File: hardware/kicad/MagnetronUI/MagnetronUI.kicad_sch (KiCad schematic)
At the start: 10 parts, among them J1 Conn_01x04, J2 Conn_02x13_Counter_Clockwise, SW1 SW_Push, SW2 SW_Push

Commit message: feat: cleanup
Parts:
- removed C1, C2: C, Capacitor_SMD:C_0805_2012Metric_Pad1.18x1.45mm_HandSolder, symbol Device:C
- removed R1, R2, R3, R4: R, Resistor_SMD:R_0805_2012Metric_Pad1.20x1.40mm_HandSolder, symbol Device:R
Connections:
- net aux1_btn: now also SW2.1
- net aux2_btn: now also SW1.1

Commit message: feat: updates
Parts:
- removed SW2: SW_Push, TerminalBlock_Phoenix:TerminalBlock_Phoenix_MKDS-1,5-2_1x02_P5.00mm_Horizontal, symbol Switch:SW_Push
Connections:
- net aux2_btn is gone; now on net aux1_btn: J2.18 (Pin_18), SW1.1
- net +3.3V: no longer J1.2 (Pin_2)
- net aux1_btn: no longer J2.17 (Pin_17)
- net +5V: now reaches J2.22 (Pin_22)
- net +5V: now also J1.2 (Pin_2)

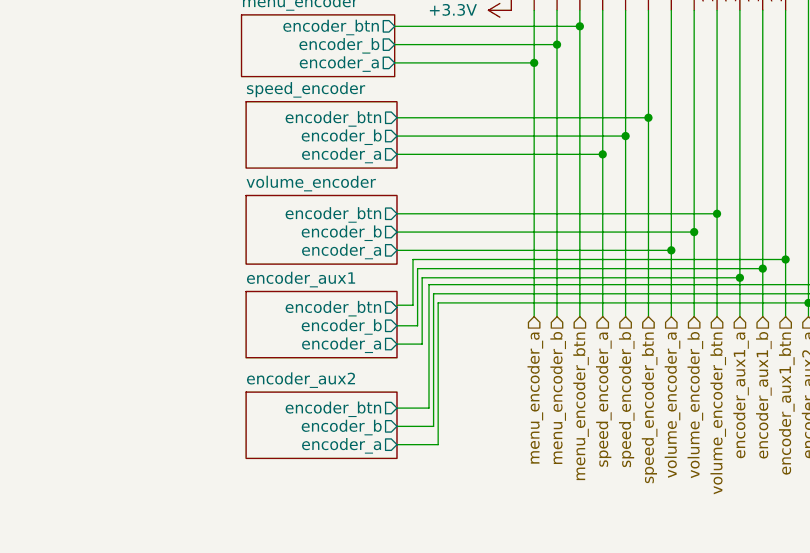
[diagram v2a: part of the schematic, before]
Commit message: feat: update to 2 layer board
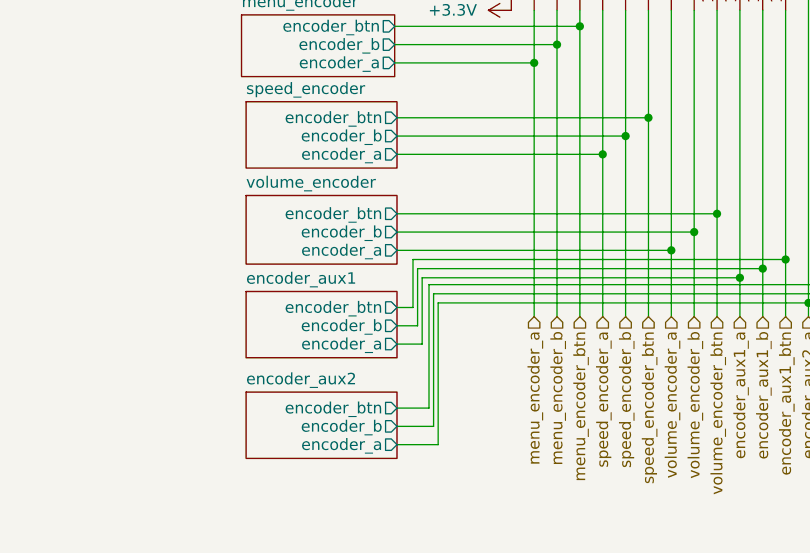
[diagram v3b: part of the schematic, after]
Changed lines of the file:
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@@
+	(wire
+		(pts
+			(xy 84.836 116.586) (xy 84.836 121.92)
+		)
+		(stroke
+			(width 0)
+			(type default)
+		)
+	)
 	(wire
 		(pts
@@
 	(wire
 		(pts
-			(xy 83.058 121.666) (xy 84.836 121.666)
-		)
-		(stroke
-			(width 0)
-			(type default)
-		)
-	)
-	(wire
-		(pts
 			(xy 144.018 122.936) (xy 144.018 60.96)
 		)
@@
 	(wire
 		(pts
+			(xy 83.058 121.92) (xy 84.836 121.92)
+		)
+		(stroke
+			(width 0)
+			(type default)
+		)
+	)
+	(wire
+		(pts
 			(xy 118.618 111.506) (xy 118.618 122.936)
 		)
@@
 		)
 		(stroke
-			(width 0)
-			(type default)
-		)
-	)
-	(wire
-		(pts
-			(xy 84.836 121.666) (xy 84.836 116.586)
-		)
-		(stroke

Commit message: chore: cleanup/mounting holes
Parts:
- added H1, H2, H3, H4: MountingHole_Pad, MountingHole:MountingHole_3.2mm_M3_ISO7380_Pad_TopBottom, symbol Mechanical:MountingHole_Pad
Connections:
- net GND: now also H1.1, H2.1, H3.1, H4.1

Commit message: chore: cleanup
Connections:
- net scl: no longer J1.4 (Pin_4)
- net sda: no longer J1.3 (Pin_3)
- new net scl_5v: J1.4 (Pin_4)
- new net sda_5v: J1.3 (Pin_3)
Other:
- added sheet level_shifter (level_shifter.kicad_sch)
- added sheet level_shifter1 (level_shifter.kicad_sch)
- moved on the sheet: J1, J2, SW1
